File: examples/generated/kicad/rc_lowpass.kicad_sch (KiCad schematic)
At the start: 3 parts

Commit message: Attempt to create legible symbols.
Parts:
- C1: symbol examples:CAP -> CAP
- R1: symbol examples:R -> R
- V1: symbol examples:VSOURCE -> VSOURCE
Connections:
- net GND: now also C1.2, V1.1 (E1)
- new net: R1.1, V1.2 (E2)
- new net: C1.1, R1.2
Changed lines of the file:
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@@
     (comment 1 "Generated by mixedsig2cad")
   )
-  (symbol (lib_id "examples:VSOURCE") (at 50.00 55.00 0) (unit 1)
+  (symbol (lib_id "VSOURCE") (at 50.00 55.00 0) (unit 1)
     (in_bom yes) (on_board yes)
     (property "Reference" "V1" (at 50.0 51.19 0)
@@
     )
   )
-  (symbol (lib_id "examples:R") (at 95.00 55.00 90) (unit 1)
+  (symbol (lib_id "R") (at 95.00 55.00 90) (unit 1)
     (in_bom yes) (on_board yes)
     (property "Reference" "R1" (at 95.0 51.19 0)
@@
     )
   )
-  (symbol (lib_id "examples:CAP") (at 95.00 90.00 90) (unit 1)
+  (symbol (lib_id "CAP") (at 95.00 90.00 90) (unit 1)
     (in_bom yes) (on_board yes)
     (property "Reference" "C1" (at 95.0 86.19 0)
@@
     )
   )
-  (symbol (lib_id "examples:GND") (at 38.00 41.38 0) (unit 1)
+  (symbol (lib_id "GND") (at 38.00 41.38 0) (unit 1)
     (in_bom yes) (on_board yes)
     (property "Reference" "#PWR0001" (at 38.0 37.57 0)

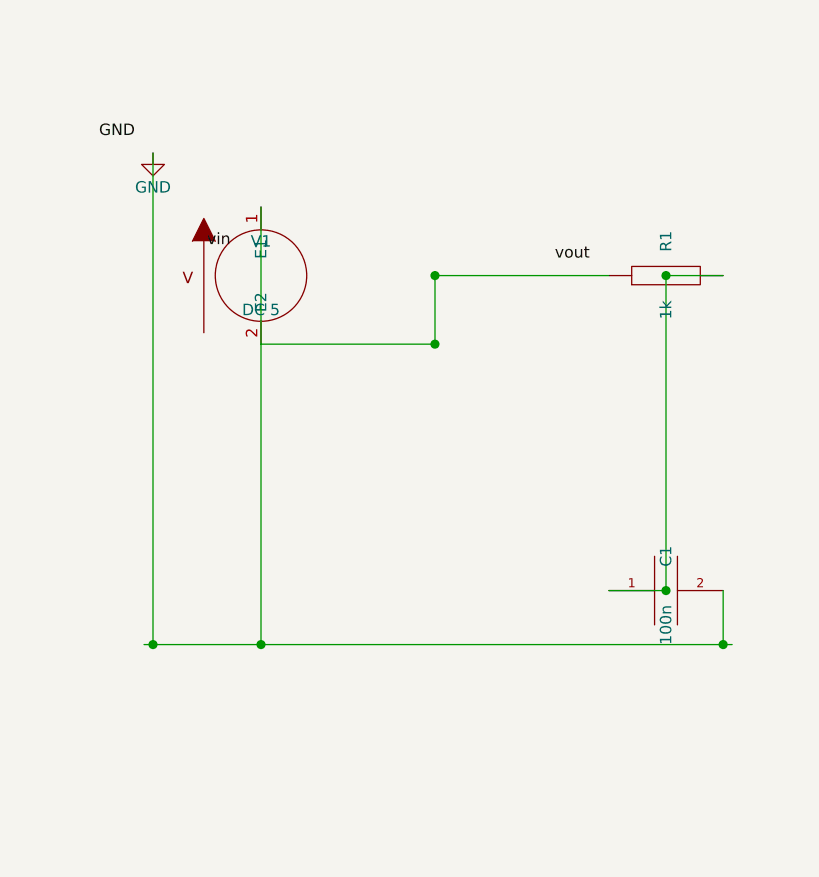
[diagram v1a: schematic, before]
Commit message: Attempt full seperation of circuit concerns into layers.
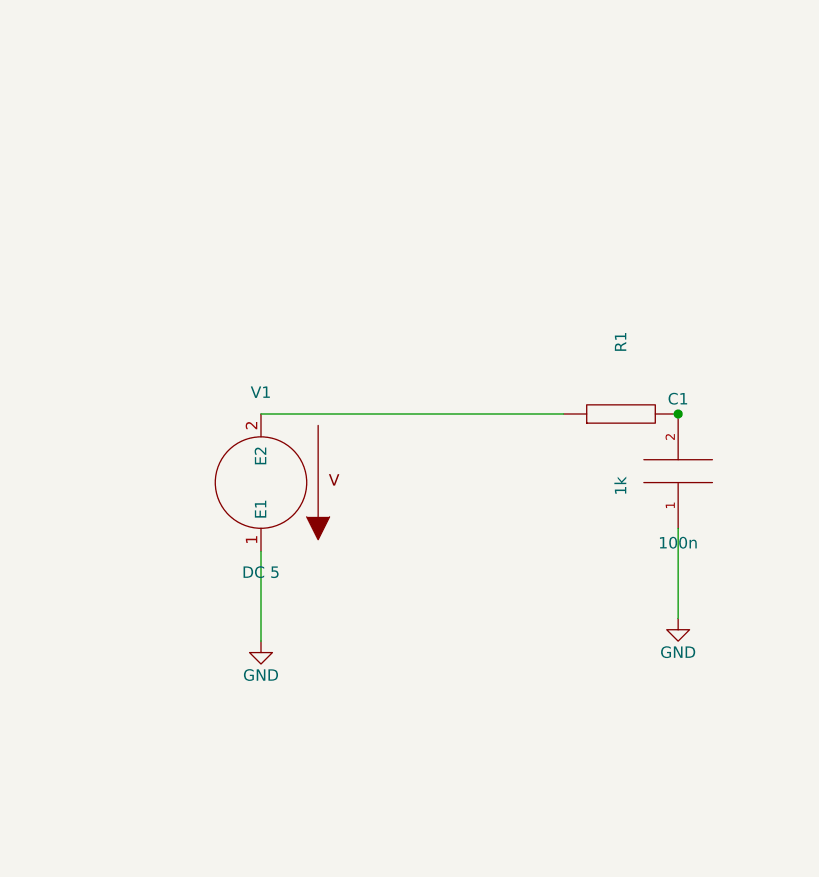
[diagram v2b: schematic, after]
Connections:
- net GND: now also C1.1; no longer C1.2
- net at R1.2: now also C1.2; no longer C1.1
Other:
- moved on the sheet: C1, R1, V1
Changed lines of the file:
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@@
   (title_block
     (title "rc_lowpass")
-    (date "2026-03-05")
+    (date "2026-03-06")
     (comment 1 "Generated by mixedsig2cad")
   )
-  (symbol (lib_id "VSOURCE") (at 50.00 55.00 0) (unit 1)
+  (symbol (lib_id "VSOURCE") (at 50.00 78.00 180) (unit 1)
     (in_bom yes) (on_board yes)
-    (property "Reference" "V1" (at 50.0 51.19 0)
+    (property "Reference" "V1" (at 50.0 68.0 0)
       (effects (font (size 1.27 1.27)))
     )
-    (property "Value" "DC 5" (at 50.0 58.81 0)
+    (property "Value" "DC 5" (at 50.0 88.0 0)
       (effects (font (size 1.27 1.27)))
     )
@@
     )
   )
-  (symbol (lib_id "R") (at 95.00 55.00 90) (unit 1)
+  (symbol (lib_id "R") (at 90.00 70.38 90) (unit 1)
     (in_bom yes) (on_board yes)
-    (property "Reference" "R1" (at 95.0 51.19 0)
+    (property "Reference" "R1" (at 90.0 62.379999999999995 0)
       (effects (font (size 1.27 1.27)))
     )
-    (property "Value" "1k" (at 95.0 58.81 0)
+    (property "Value" "1k" (at 90.0 78.38 0)
       (effects (font (size 1.27 1.27)))
     )
@@
     )
   )
-  (symbol (lib_id "CAP") (at 95.00 90.00 90) (unit 1)
+  (symbol (lib_id "CAP") (at 96.35 76.73 180) (unit 1)
     (in_bom yes) (on_board yes)
-    (property "Reference" "C1" (at 95.0 86.19 0)
+    (property "Reference" "C1" (at 96.35 68.73 0)
       (effects (font (size 1.27 1.27)))
     )
-    (property "Value" "100n" (at 95.0 93.81 0)
+    (property "Value" "100n" (at 96.35 84.73 0)
       (effects (font (size 1.27 1.27)))
     )
@@
     )
   )
-  (symbol (lib_id "GND") (at 38.00 41.38 0) (unit 1)
+  (symbol (lib_id "GND") (at 50.00 95.62 0) (unit 1)
     (in_bom yes) (on_board yes)
-    (property "Reference" "#PWR0001" (at 38.0 37.57 0)
+    (property "Reference" "#PWR0001" (at 50.0 91.81 0)
       (effects (font (size 1.27 1.27)) hide)
     )
-    (property "Value" "GND" (at 38.0 45.190000000000005 0)
+    (property "Value" "GND" (at 50.0 99.43 0)
       (effects (font (size 1.27 1.27)))
     )
@@
     )
   )
-  (label "GND" (at 32.00 39.88 0)
-    (effects (font (size 1.27 1.27)) (justify left bottom))
+  (symbol (lib_id "GND") (at 96.35 93.08 0) (unit 1)
+    (in_bom yes) (on_board yes)
+    (property "Reference" "#PWR0002" (at 96.35 89.27 0)
+      (effects (font (size 1.27 1.27)) hide)
+    )
+    (property "Value" "GND" (at 96.35 96.89 0)
+      (effects (font (size 1.27 1.27)))
+    )
+    (property "Footprint" "" (at 0 0 0)
+      (effects (font (size 1.27 1.27)) hide)
+    )
+    (property "Datasheet" "" (at 0 0 0)
+      (effects (font (size 1.27 1.27)) hide)
+    )
   )
-  (label "vin" (at 44.00 52.00 0)
-    (effects (font (size 1.27 1.27)) (justify left bottom))
-  )
-  (label "vout" (at 82.65 53.50 0)
-    (effects (font (size 1.27 1.27)) (justify left bottom))
-  )
-  (wire (pts (xy 37.00 96.00) (xy 102.35 96.00))
+  (wire (pts (xy 50.00 70.38) (xy 83.65 70.38))
     (stroke (width 0) (type solid) (color 0 0 0 0))
   )
-  (wire (pts (xy 50.00 47.38) (xy 50.00 96.00))
+  (wire (pts (xy 50.00 85.62) (xy 50.00 95.62))
     (stroke (width 0) (type solid) (color 0 0 0 0))
   )
-  (wire (pts (xy 101.35 90.00) (xy 101.35 96.00))
+  (wire (pts (xy 96.35 83.08) (xy 96.35 93.08))
     (stroke (width 0) (type solid) (color 0 0 0 0))
   )
-  (wire (pts (xy 38.00 41.38) (xy 38.00 96.00))
-    (stroke (width 0) (type solid) (color 0 0 0 0))
-  )
-  (wire (pts (xy 50.00 62.62) (xy 69.33 62.62))
-    (stroke (width 0) (type solid) (color 0 0 0 0))
-  )
-  (wire (pts (xy 69.33 62.62) (xy 69.33 55.00))
-    (stroke (width 0) (type solid) (color 0 0 0 0))
-  )
-  (wire (pts (xy 69.33 55.00) (xy 88.65 55.00))
-    (stroke (width 0) (type solid) (color 0 0 0 0))
-  )
-  (wire (pts (xy 101.35 55.00) (xy 95.00 55.00))
-    (stroke (width 0) (type solid) (color 0 0 0 0))
-  )
-  (wire (pts (xy 95.00 55.00) (xy 95.00 90.00))
-    (stroke (width 0) (type solid) (color 0 0 0 0))
-  )
-  (wire (pts (xy 95.00 90.00) (xy 88.65 90.00))
-    (stroke (width 0) (type solid) (color 0 0 0 0))
-  )
-  (junction (at 50.00 96.00) (diameter 1.016) (color 0 0 0 0))
-  (junction (at 101.35 96.00) (diameter 1.016) (color 0 0 0 0))
-  (junction (at 38.00 96.00) (diameter 1.016) (color 0 0 0 0))
-  (junction (at 69.33 62.62) (diameter 1.016) (color 0 0 0 0))
-  (junction (at 69.33 55.00) (diameter 1.016) (color 0 0 0 0))
-  (junction (at 95.00 55.00) (diameter 1.016) (color 0 0 0 0))
-  (junction (at 95.00 90.00) (diameter 1.016) (color 0 0 0 0))
+  (junction (at 96.35 70.38) (diameter 1.016) (color 0 0 0 0))
   (sheet_instances
     (path "/" (page "1"))
@@
     (path "/f9364b86-dfb1-51e8-9247-72a2484cf109" (reference "R1") (unit 1) (value "1k") (footprint ""))
     (path "/fff04eb7-92e3-5e3e-9950-c8b8ac3c6096" (reference "C1") (unit 1) (value "100n") (footprint ""))
-    (path "/4d746a25-6e32-5362-9bf4-cd3363ff6631" (reference "#PWR0001") (unit 1) (value "GND") (footprint ""))
+    (path "/99395be3-a0e4-5d09-bc7f-547778482ecc" (reference "#PWR0001") (unit 1) (value "GND") (footprint ""))
+    (path "/662a2282-d2d1-5b8b-9fa8-19311be8b5b1" (reference "#PWR0002") (unit 1) (value "GND") (footprint ""))
   )
 )

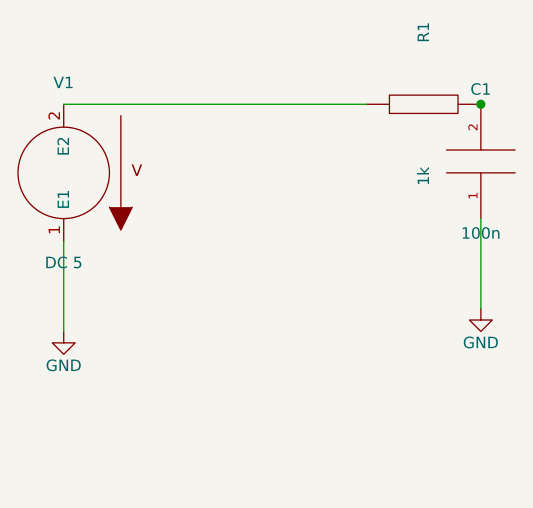
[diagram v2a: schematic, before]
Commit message: Add checks for connectivity.
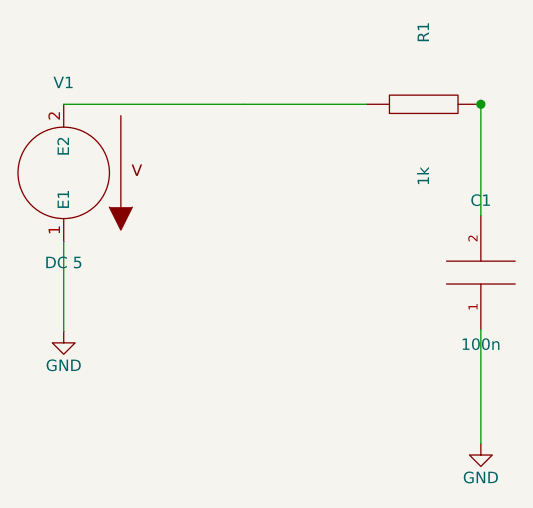
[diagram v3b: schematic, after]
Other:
- moved on the sheet: C1
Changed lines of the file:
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@@
     )
   )
-  (symbol (lib_id "CAP") (at 96.35 76.73 180) (unit 1)
+  (symbol (lib_id "CAP") (at 96.35 89.08 180) (unit 1)
     (in_bom yes) (on_board yes)
-    (property "Reference" "C1" (at 96.35 68.73 0)
+    (property "Reference" "C1" (at 96.35 81.08 0)
       (effects (font (size 1.27 1.27)))
     )
-    (property "Value" "100n" (at 96.35 84.73 0)
+    (property "Value" "100n" (at 96.35 97.08 0)
       (effects (font (size 1.27 1.27)))
     )
@@
     )
   )
-  (symbol (lib_id "GND") (at 96.35 93.08 0) (unit 1)
+  (symbol (lib_id "GND") (at 96.35 108.08 0) (unit 1)
     (in_bom yes) (on_board yes)
-    (property "Reference" "#PWR0002" (at 96.35 89.27 0)
+    (property "Reference" "#PWR0002" (at 96.35 104.27 0)
       (effects (font (size 1.27 1.27)) hide)
     )
-    (property "Value" "GND" (at 96.35 96.89 0)
+    (property "Value" "GND" (at 96.35 111.89 0)
       (effects (font (size 1.27 1.27)))
     )
@@
     )
   )
-  (wire (pts (xy 50.00 70.38) (xy 83.65 70.38))
+  (wire (pts (xy 50.00 70.38) (xy 70.00 70.38))
+    (stroke (width 0) (type solid) (color 0 0 0 0))
+  )
+  (wire (pts (xy 83.65 70.38) (xy 70.00 70.38))
+    (stroke (width 0) (type solid) (color 0 0 0 0))
+  )
+  (wire (pts (xy 96.35 82.73) (xy 96.35 70.38))
     (stroke (width 0) (type solid) (color 0 0 0 0))
   )
@@
     (stroke (width 0) (type solid) (color 0 0 0 0))
   )
-  (wire (pts (xy 96.35 83.08) (xy 96.35 93.08))
+  (wire (pts (xy 96.35 95.43) (xy 96.35 108.08))
     (stroke (width 0) (type solid) (color 0 0 0 0))
   )

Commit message: Attempt to correct strange wiring.
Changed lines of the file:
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@@
     )
   )
-  (wire (pts (xy 50.00 70.38) (xy 70.00 70.38))
+  (wire (pts (xy 50.00 70.38) (xy 83.65 70.38))
     (stroke (width 0) (type solid) (color 0 0 0 0))
   )
-  (wire (pts (xy 83.65 70.38) (xy 70.00 70.38))
-    (stroke (width 0) (type solid) (color 0 0 0 0))
-  )

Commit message: Attempt shape and wiring fixes again.
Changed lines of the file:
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@@
     (stroke (width 0) (type solid) (color 0 0 0 0))
   )
-  (wire (pts (xy 50.00 85.62) (xy 50.00 95.62))
+  (wire (pts (xy 50.00 85.62) (xy 50.00 87.50))
     (stroke (width 0) (type solid) (color 0 0 0 0))
   )
-  (wire (pts (xy 96.35 95.43) (xy 96.35 108.08))
+  (wire (pts (xy 50.00 87.50) (xy 56.00 87.50))
     (stroke (width 0) (type solid) (color 0 0 0 0))
   )
+  (wire (pts (xy 56.00 87.50) (xy 56.00 95.62))
+    (stroke (width 0) (type solid) (color 0 0 0 0))
+  )
+  (wire (pts (xy 56.00 95.62) (xy 50.00 95.62))
+    (stroke (width 0) (type solid) (color 0 0 0 0))
+  )
+  (wire (pts (xy 96.35 95.43) (xy 96.35 101.08))
+    (stroke (width 0) (type solid) (color 0 0 0 0))
+  )
+  (wire (pts (xy 96.35 101.08) (xy 102.35 101.08))
+    (stroke (width 0) (type solid) (color 0 0 0 0))
+  )
+  (wire (pts (xy 102.35 101.08) (xy 102.35 108.08))
+    (stroke (width 0) (type solid) (color 0 0 0 0))
+  )
+  (wire (pts (xy 102.35 108.08) (xy 96.35 108.08))
+    (stroke (width 0) (type solid) (color 0 0 0 0))
+  )

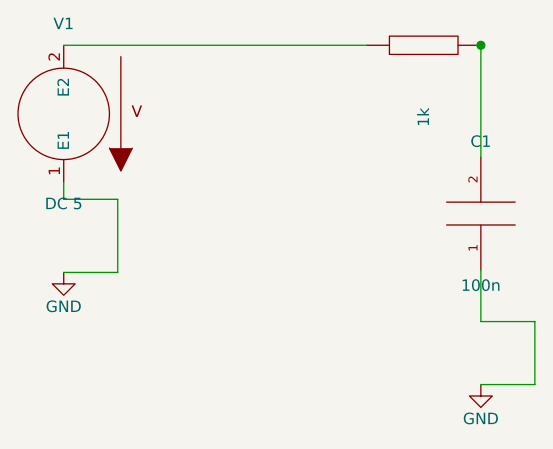
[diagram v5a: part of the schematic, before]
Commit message: Attempt to fix kinking and terminal direction issuses.
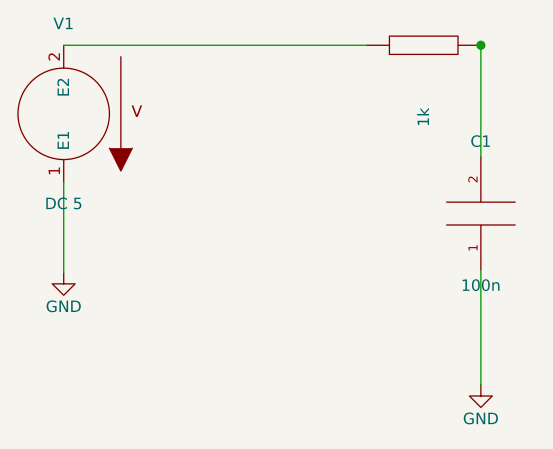
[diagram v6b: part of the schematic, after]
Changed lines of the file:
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@@
     (stroke (width 0) (type solid) (color 0 0 0 0))
   )
-  (wire (pts (xy 50.00 85.62) (xy 50.00 87.50))
+  (wire (pts (xy 50.00 85.62) (xy 50.00 95.62))
     (stroke (width 0) (type solid) (color 0 0 0 0))
   )
-  (wire (pts (xy 50.00 87.50) (xy 56.00 87.50))
+  (wire (pts (xy 96.35 95.43) (xy 96.35 108.08))
     (stroke (width 0) (type solid) (color 0 0 0 0))
   )
-  (wire (pts (xy 56.00 87.50) (xy 56.00 95.62))
-    (stroke (width 0) (type solid) (color 0 0 0 0))
-  )
-  (wire (pts (xy 56.00 95.62) (xy 50.00 95.62))
-    (stroke (width 0) (type solid) (color 0 0 0 0))
-  )
-  (wire (pts (xy 96.35 95.43) (xy 96.35 101.08))
-    (stroke (width 0) (type solid) (color 0 0 0 0))
-  )
-  (wire (pts (xy 96.35 101.08) (xy 102.35 101.08))
-    (stroke (width 0) (type solid) (color 0 0 0 0))
-  )
-  (wire (pts (xy 102.35 101.08) (xy 102.35 108.08))
-    (stroke (width 0) (type solid) (color 0 0 0 0))
-  )
-  (wire (pts (xy 102.35 108.08) (xy 96.35 108.08))
-    (stroke (width 0) (type solid) (color 0 0 0 0))
-  )

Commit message: Attempt to fix more terminal issues.
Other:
- moved on the sheet: C1, R1, V1
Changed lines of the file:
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@@
     (comment 1 "Generated by mixedsig2cad")
   )
-  (symbol (lib_id "VSOURCE") (at 50.00 78.00 180) (unit 1)
+  (symbol (lib_id "VSOURCE") (at 56.00 86.00 180) (unit 1)
     (in_bom yes) (on_board yes)
-    (property "Reference" "V1" (at 50.0 68.0 0)
+    (property "Reference" "V1" (at 56.0 76.0 0)
       (effects (font (size 1.27 1.27)))
     )
-    (property "Value" "DC 5" (at 50.0 88.0 0)
+    (property "Value" "DC 5" (at 56.0 96.0 0)
       (effects (font (size 1.27 1.27)))
     )
@@
     )
   )
-  (symbol (lib_id "R") (at 90.00 70.38 90) (unit 1)
+  (symbol (lib_id "GND") (at 56.00 105.62 0) (unit 1)
     (in_bom yes) (on_board yes)
-    (property "Reference" "R1" (at 90.0 62.379999999999995 0)
-      (effects (font (size 1.27 1.27)))
+    (property "Reference" "#PWR0001" (at 56.0 101.81 0)
+      (effects (font (size 1.27 1.27)) hide)
     )
-    (property "Value" "1k" (at 90.0 78.38 0)
+    (property "Value" "GND" (at 56.0 109.43 0)
       (effects (font (size 1.27 1.27)))
     )
@@
     )
   )
-  (symbol (lib_id "CAP") (at 96.35 89.08 180) (unit 1)
+  (symbol (lib_id "R") (at 90.00 78.00 90) (unit 1)
     (in_bom yes) (on_board yes)
-    (property "Reference" "C1" (at 96.35 81.08 0)
+    (property "Reference" "R1" (at 90.0 70.0 0)
       (effects (font (size 1.27 1.27)))
     )
-    (property "Value" "100n" (at 96.35 97.08 0)
+    (property "Value" "1k" (at 90.0 86.0 0)
       (effects (font (size 1.27 1.27)))
     )
@@
     )
   )
-  (symbol (lib_id "GND") (at 50.00 95.62 0) (unit 1)
+  (symbol (lib_id "CAP") (at 96.35 96.35 180) (unit 1)
     (in_bom yes) (on_board yes)
-    (property "Reference" "#PWR0001" (at 50.0 91.81 0)
-      (effects (font (size 1.27 1.27)) hide)
+    (property "Reference" "C1" (at 96.35 88.35 0)
+      (effects (font (size 1.27 1.27)))
     )
-    (property "Value" "GND" (at 50.0 99.43 0)
+    (property "Value" "100n" (at 96.35 104.35 0)
       (effects (font (size 1.27 1.27)))
     )
@@
     )
   )
-  (symbol (lib_id "GND") (at 96.35 108.08 0) (unit 1)
+  (symbol (lib_id "GND") (at 96.35 114.70 0) (unit 1)
     (in_bom yes) (on_board yes)
-    (property "Reference" "#PWR0002" (at 96.35 104.27 0)
+    (property "Reference" "#PWR0002" (at 96.35 110.89 0)
       (effects (font (size 1.27 1.27)) hide)
     )
-    (property "Value" "GND" (at 96.35 111.89 0)
+    (property "Value" "GND" (at 96.35 118.51 0)
       (effects (font (size 1.27 1.27)))
     )
@@
     )
   )
-  (wire (pts (xy 50.00 70.38) (xy 83.65 70.38))
+  (wire (pts (xy 96.35 102.70) (xy 96.35 114.70))
     (stroke (width 0) (type solid) (color 0 0 0 0))
   )
-  (wire (pts (xy 96.35 82.73) (xy 96.35 70.38))
+  (wire (pts (xy 56.00 93.62) (xy 56.00 105.62))
     (stroke (width 0) (type solid) (color 0 0 0 0))
   )
-  (wire (pts (xy 50.00 85.62) (xy 50.00 95.62))
+  (wire (pts (xy 56.00 78.38) (xy 56.00 78.00))
     (stroke (width 0) (type solid) (color 0 0 0 0))
   )
-  (wire (pts (xy 96.35 95.43) (xy 96.35 108.08))
+  (wire (pts (xy 56.00 78.00) (xy 83.65 78.00))
     (stroke (width 0) (type solid) (color 0 0 0 0))
   )
-  (junction (at 96.35 70.38) (diameter 1.016) (color 0 0 0 0))
+  (wire (pts (xy 96.35 78.00) (xy 96.35 90.00))
+    (stroke (width 0) (type solid) (color 0 0 0 0))
+  )
   (sheet_instances
     (path "/" (page "1"))
@@
   (symbol_instances
     (path "/c171cc21-d2ba-581e-8446-b23465a59c7b" (reference "V1") (unit 1) (value "DC 5") (footprint ""))
+    (path "/99395be3-a0e4-5d09-bc7f-547778482ecc" (reference "#PWR0001") (unit 1) (value "GND") (footprint ""))
     (path "/f9364b86-dfb1-51e8-9247-72a2484cf109" (reference "R1") (unit 1) (value "1k") (footprint ""))
     (path "/fff04eb7-92e3-5e3e-9950-c8b8ac3c6096" (reference "C1") (unit 1) (value "100n") (footprint ""))
-    (path "/99395be3-a0e4-5d09-bc7f-547778482ecc" (reference "#PWR0001") (unit 1) (value "GND") (footprint ""))
     (path "/662a2282-d2d1-5b8b-9fa8-19311be8b5b1" (reference "#PWR0002") (unit 1) (value "GND") (footprint ""))
   )
